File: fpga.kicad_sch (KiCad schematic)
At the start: 32 parts, among them Q1 BSS138PW, SW1 SW_B3U-1000P_SMD, U1 ICE40UP5K-SG48, U2 W25Q32JW_SOIC-8, Y1 Oscillator_12MHz_ESC_2520MV

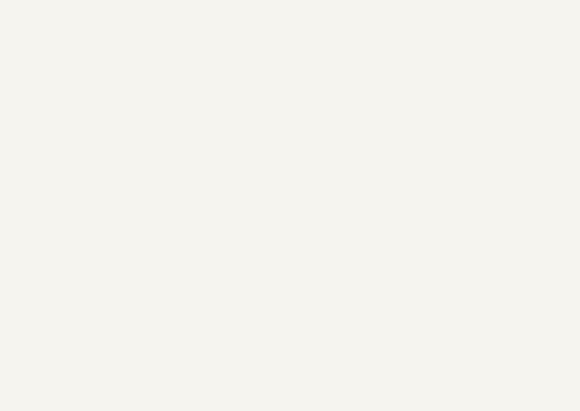
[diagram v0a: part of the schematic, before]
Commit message: [#72133] Add rough schematic hierarchy
Signed-off-by: Dawid Lentka <dlentka@antmicro.com>
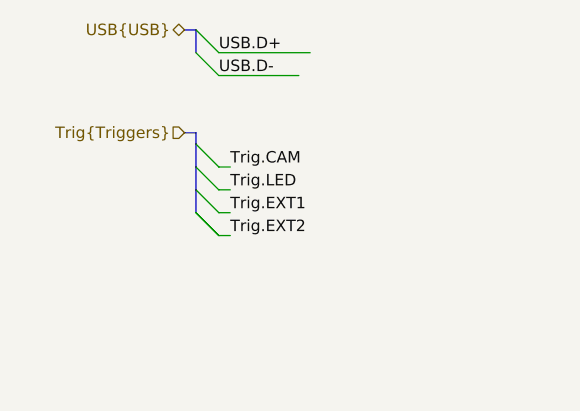
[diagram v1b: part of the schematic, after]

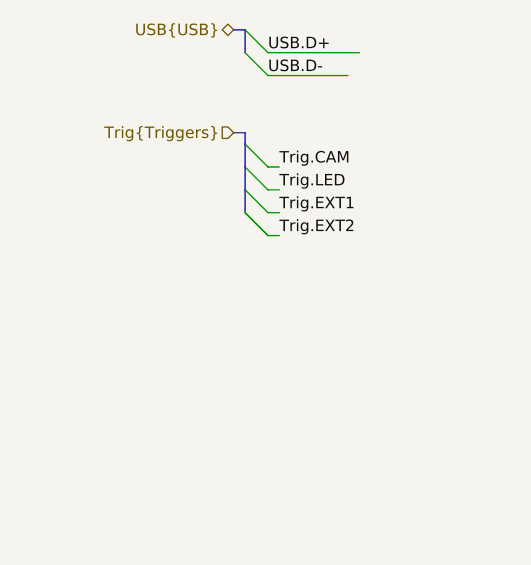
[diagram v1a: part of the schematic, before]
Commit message: [#72133] Add USB mux
Signed-off-by: Dawid Lentka <dlentka@antmicro.com>
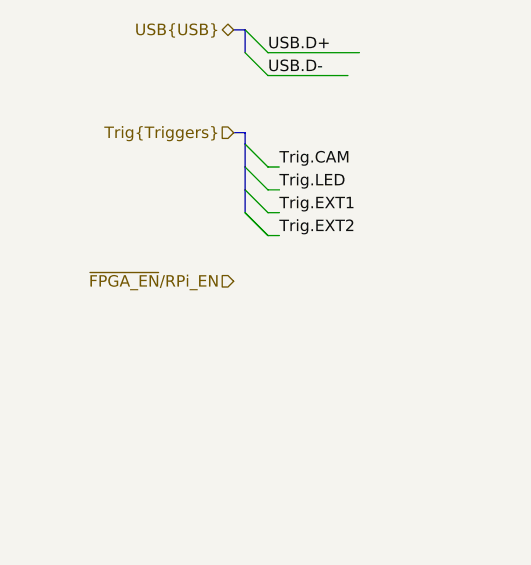
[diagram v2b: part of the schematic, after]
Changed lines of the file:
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@@
+		)
+	)
+	(hierarchical_label "~{FPGA_EN}{slash}RPi_EN"
+		(shape input)
+		(at 57.15 74.93 180)
+		(fields_autoplaced yes)
+		(effects
+			(font
+				(size 1.27 1.27)
+			)
+			(justify right)
 		)
 	)

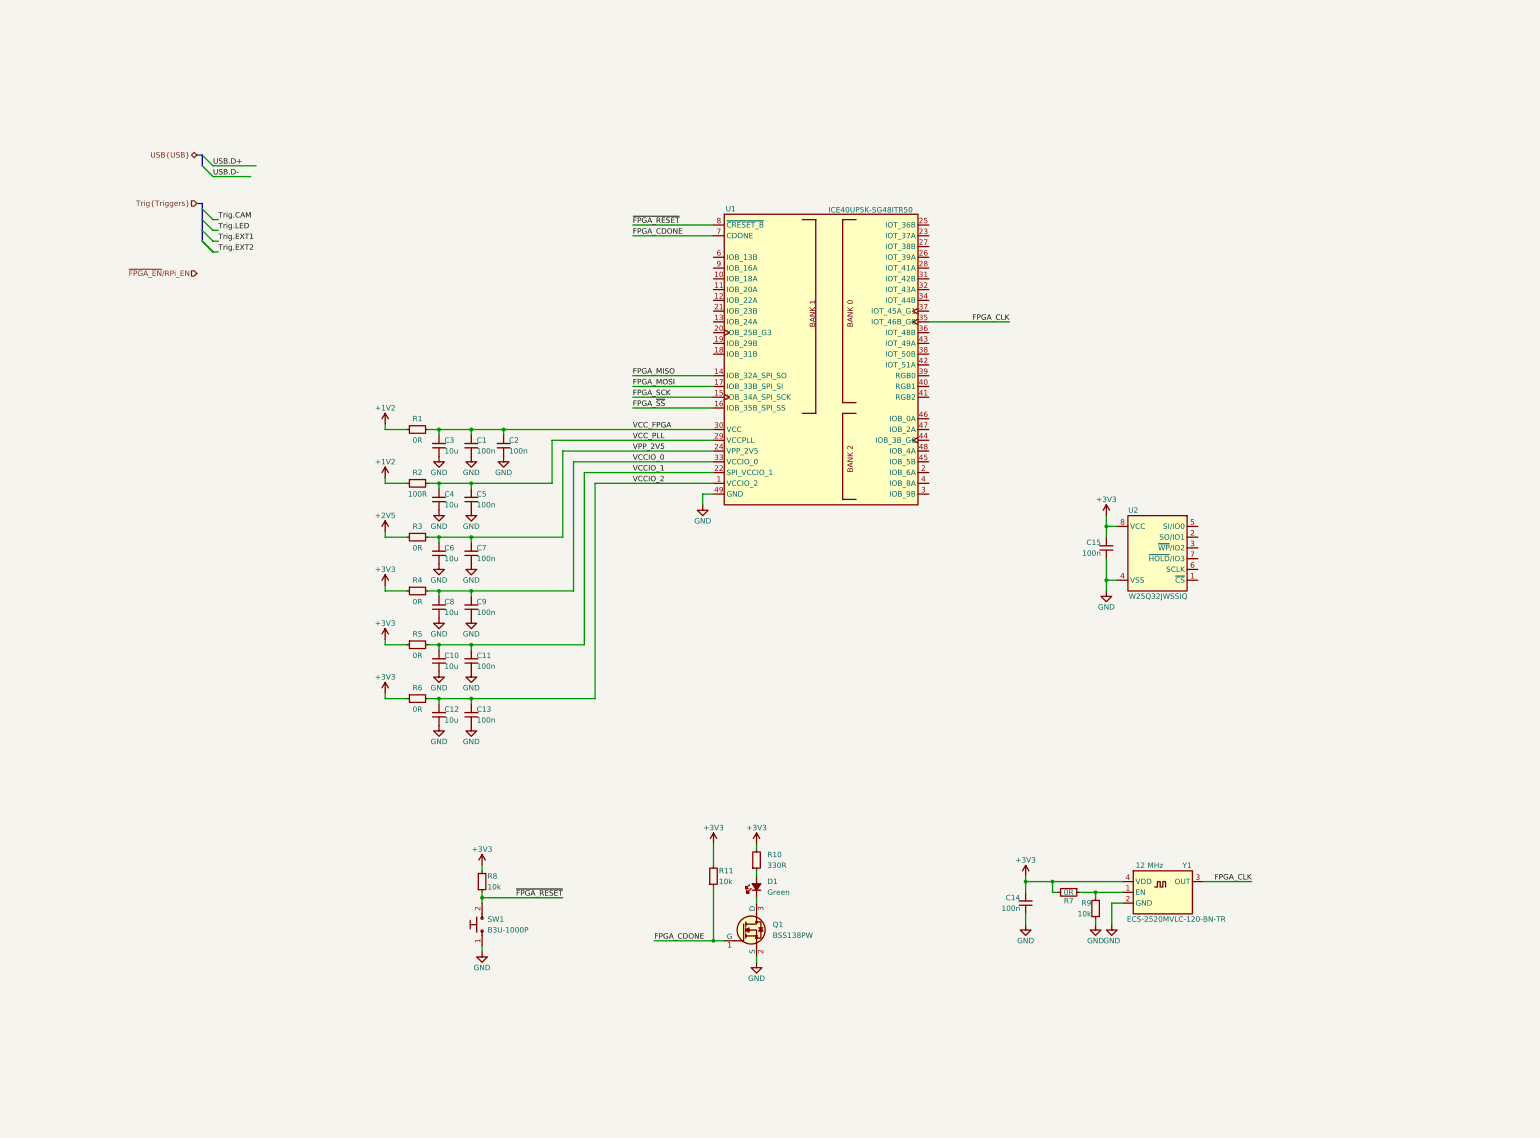
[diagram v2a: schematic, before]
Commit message: [#72133] Move executor switching to new scheet; Add FPGA flash programmer
Signed-off-by: Dawid Lentka <dlentka@antmicro.com>
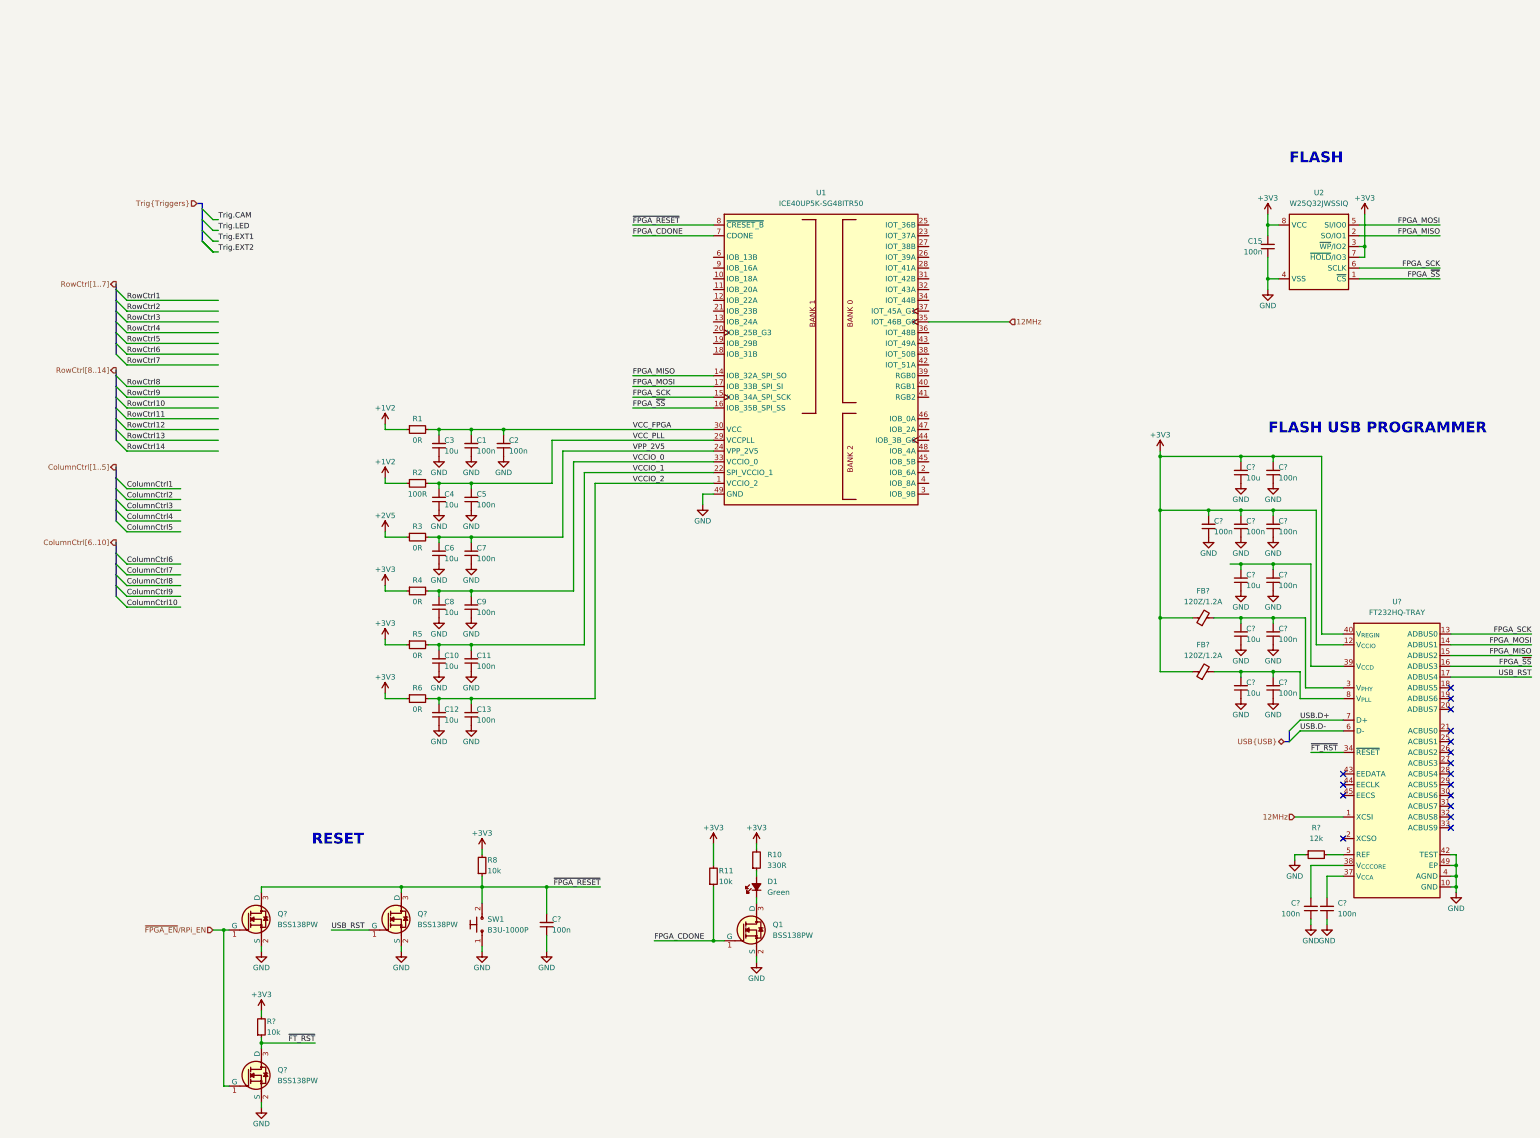
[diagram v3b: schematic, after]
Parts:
- removed C14: C_100n_0402, antmicro-footprints:C_0402_1005Metric, symbol antmicroCapacitors0402:C_100n_0402
- removed R7: R_0R_0402, antmicro-footprints:R_0402_1005Metric, symbol antmicroResistors0402:R_0R_0402
- removed R9: R_10k_0402, antmicro-footprints:R_0402_1005Metric, symbol antmicroResistors0402:R_10k_0402
- removed Y1: Oscillator_12MHz_ESC_2520MV, antmicro-footprints:Oscillator_SMD_ECS_2520MV_2.5x2mm, symbol antmicroOscillators:Oscillator_12MHz_ESC_2520MV
- added C? (x4): C_10u_10V_0402, antmicro-footprints:C_0402_1005Metric, symbol antmicroCapacitors0402:C_10u_10V_0402
- added C? (x10): C_100n_0402, antmicro-footprints:C_0402_1005Metric, symbol antmicroCapacitors0402:C_100n_0402
- added FB? (x2): FB_120Z_1.2A_TDK-MPZ_0402, antmicro-footprints:FB_0402_1005Metric, symbol antmicroFerriteBeadsandChips:FB_120Z_1.2A_TDK-MPZ_0402
- added Q? (x3): BSS138PW, antmicro-footprints:SC70-3, symbol antmicroTransistorsFETsMOSFETsSingle:BSS138PW
- added R?: R_12k_0402, antmicro-footprints:R_0402_1005Metric, symbol antmicroResistors0402:R_12k_0402
- added R?: R_10k_0402, antmicro-footprints:R_0402_1005Metric, symbol antmicroResistors0402:R_10k_0402
- added U?: FT232H_QFN, antmicro-footprints:QFN-48-1EP_8x8mm_P0.5mm_EP6.2x6.2mm_FT232HQ_marking, symbol antmicroInterfaceControllers:FT232H_QFN
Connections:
- net +3V3: now also U2.3 (~{WP}/IO2), U2.7 (~{HOLD}/IO3), C?.2, C?.2, C?.2, C?.2, C?.2, FB?.1, FB?.1, R?.2, U?.12 (V_{CCIO}), U?.24 (V_{CCIO}), U?.40 (V_{REGIN}), U?.46 (V_{CCIO})
- net FPGA_MISO: now also U2.2 (SO/IO1), U?.15 (ADBUS2)
- net FPGA_MOSI: now also U2.5 (SI/IO0), U?.14 (ADBUS1)
- net FPGA_SCK: now also U2.6 (SCLK), U?.13 (ADBUS0)
- net FPGA_~{SS}: now also U2.1 (~{CS}), U?.16 (ADBUS3)
- net GND: now also C?.1, C?.1, C?.1, C?.1, C?.1, C?.1, C?.1, C?.1, C?.1, C?.1, C?.1, C?.1, C?.1, C?.1, Q?.2 (S), Q?.2 (S), Q?.2 (S), R?.1, U?.10 (GND), U?.11 (GND), U?.22 (GND), U?.23 (GND), U?.35 (GND), U?.36 (GND), U?.4 (AGND), U?.41 (AGND), U?.42 (TEST), U?.47 (GND), U?.48 (GND), U?.49 (EP), U?.9 (AGND)
- net USB.D+: now also U?.7 (D+)
- net USB.D-: now also U?.6 (D-)
- net ~{FPGA_EN}/RPi_EN: now also Q?.1 (G), Q?.1 (G)
- net ~{FPGA_RESET}: now also C?.2, Q?.3 (D), Q?.3 (D)
- net FPGA_CLK renamed 12MHz
- net 12MHz: now also U?.1 (XCSI)
- new net: C?.2, C?.2, FB?.2, U?.8 (V_{PLL})
- new net: R?.2, U?.5 (REF)
- new net: C?.2, C?.2, U?.39 (V_{CCD})
- new net: C?.2, C?.2, FB?.2, U?.3 (V_{PHY})
- new net: C?.2, U?.37 (V_{CCA})
- new net: C?.2, U?.38 (V_{CCCORE})
- new net USB_RST: Q?.1 (G), U?.17 (ADBUS4)
- new net ~{FT_RST}: Q?.3 (D), R?.1, U?.34 (~{RESET})
- no-connect marks 0 -> 17
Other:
- note added: "FLASH"
- note added: "FLASH USB PROGRAMMER"
- note added: "RESET"
- moved on the sheet: C15, R8, U2

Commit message: [#72133] Unify sheet size
Signed-off-by: Dawid Lentka <dlentka@antmicro.com>
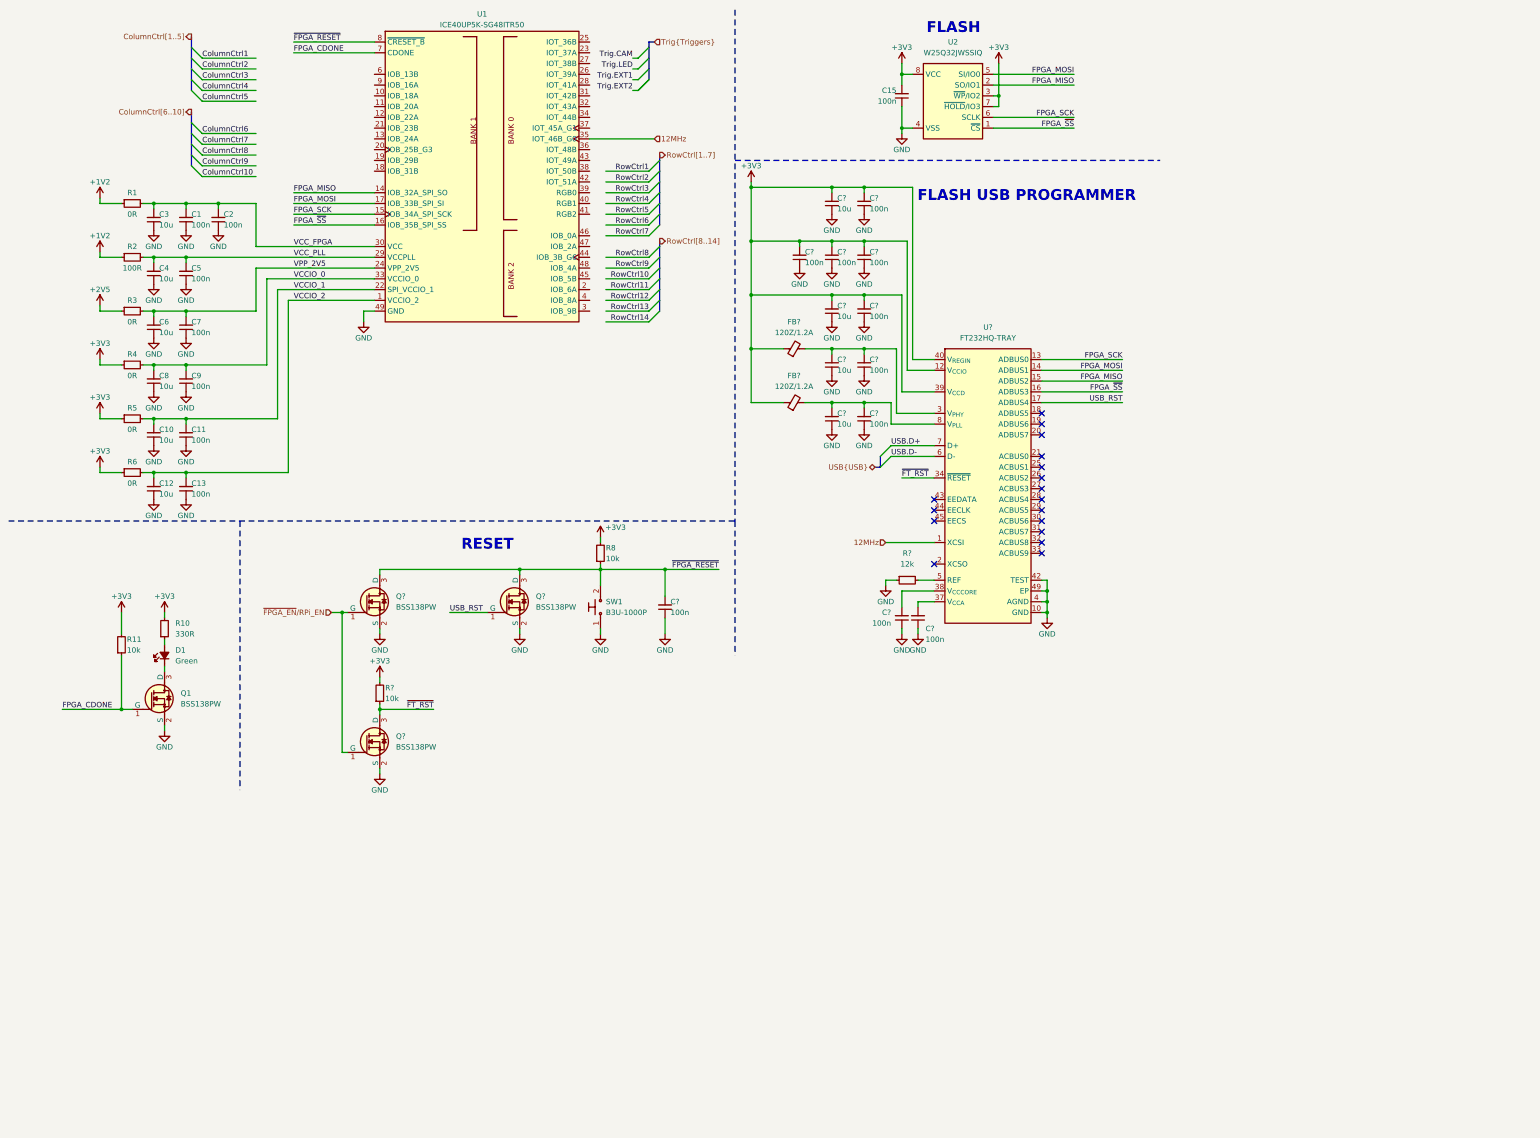
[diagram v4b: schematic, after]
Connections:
- net +3V3: now also C?.2, C?.2, U?.39 (V_{CCD})
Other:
- title: LED Panel -> LED Panel Board
- moved on the sheet: C1, C10, C11, C12, C13, C15, C2, C3, C4, C5, C6, C7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

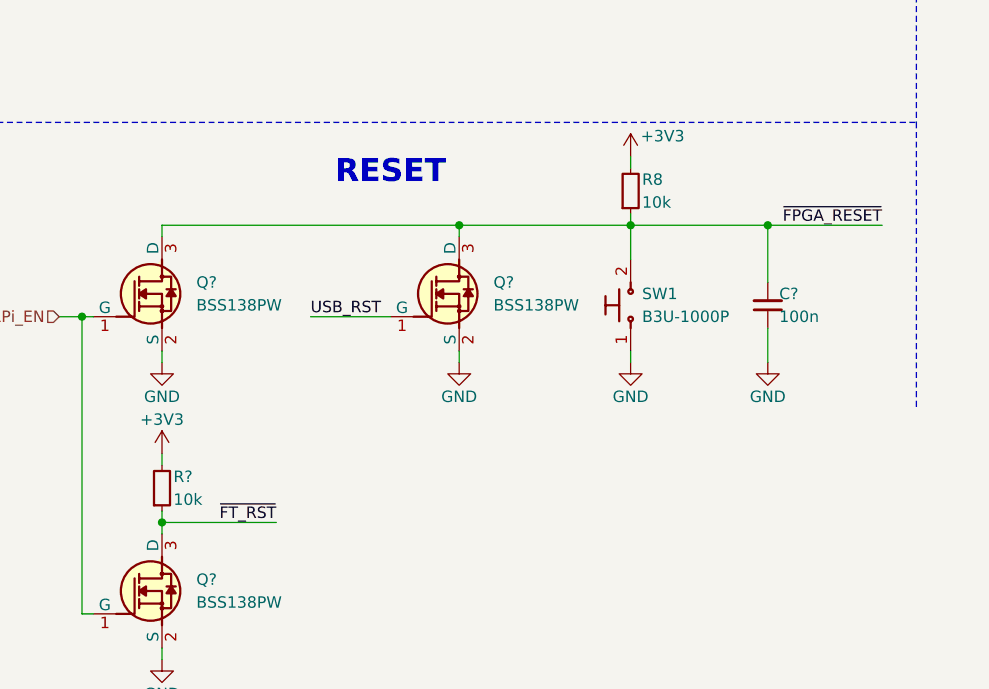
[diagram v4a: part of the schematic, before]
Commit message: [#72133] Add indicator LEDs & testpoints
Signed-off-by: Dawid Lentka <dlentka@antmicro.com>
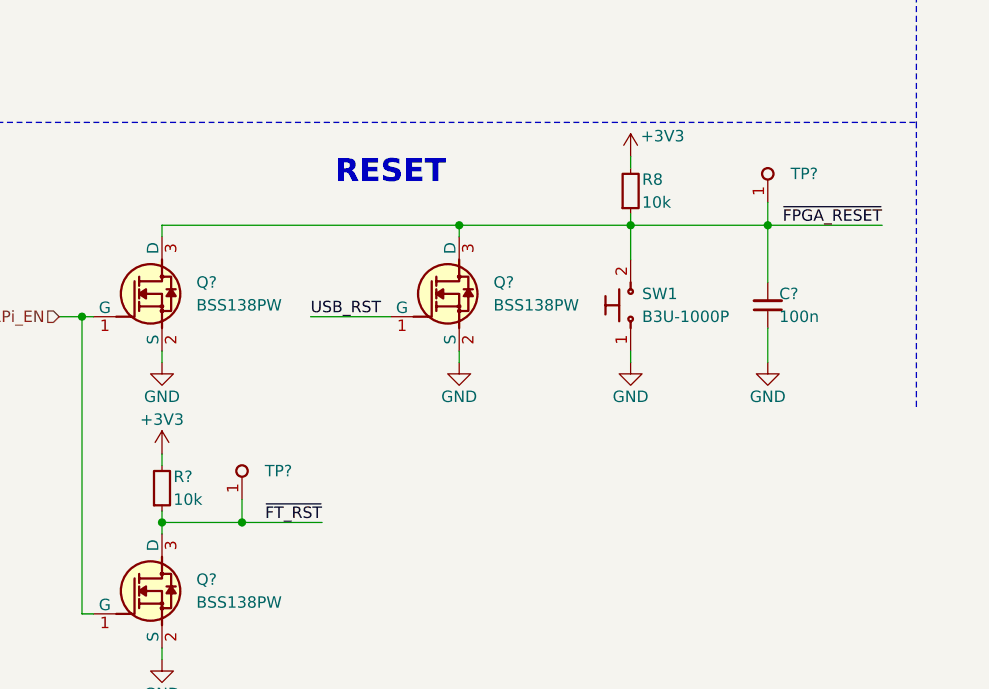
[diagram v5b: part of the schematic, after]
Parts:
- added TP? (x2): TP_0.75mm_SMD, antmicro-footprints:TP_SMD_0.75mm, symbol antmicroTestPoints:TP_0.75mm_SMD
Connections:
- net ~{FPGA_RESET}: now also TP?.1
- net ~{FT_RST}: now also TP?.1
